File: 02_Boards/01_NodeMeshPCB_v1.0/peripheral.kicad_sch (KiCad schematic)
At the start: 3 parts, among them U1 BME280

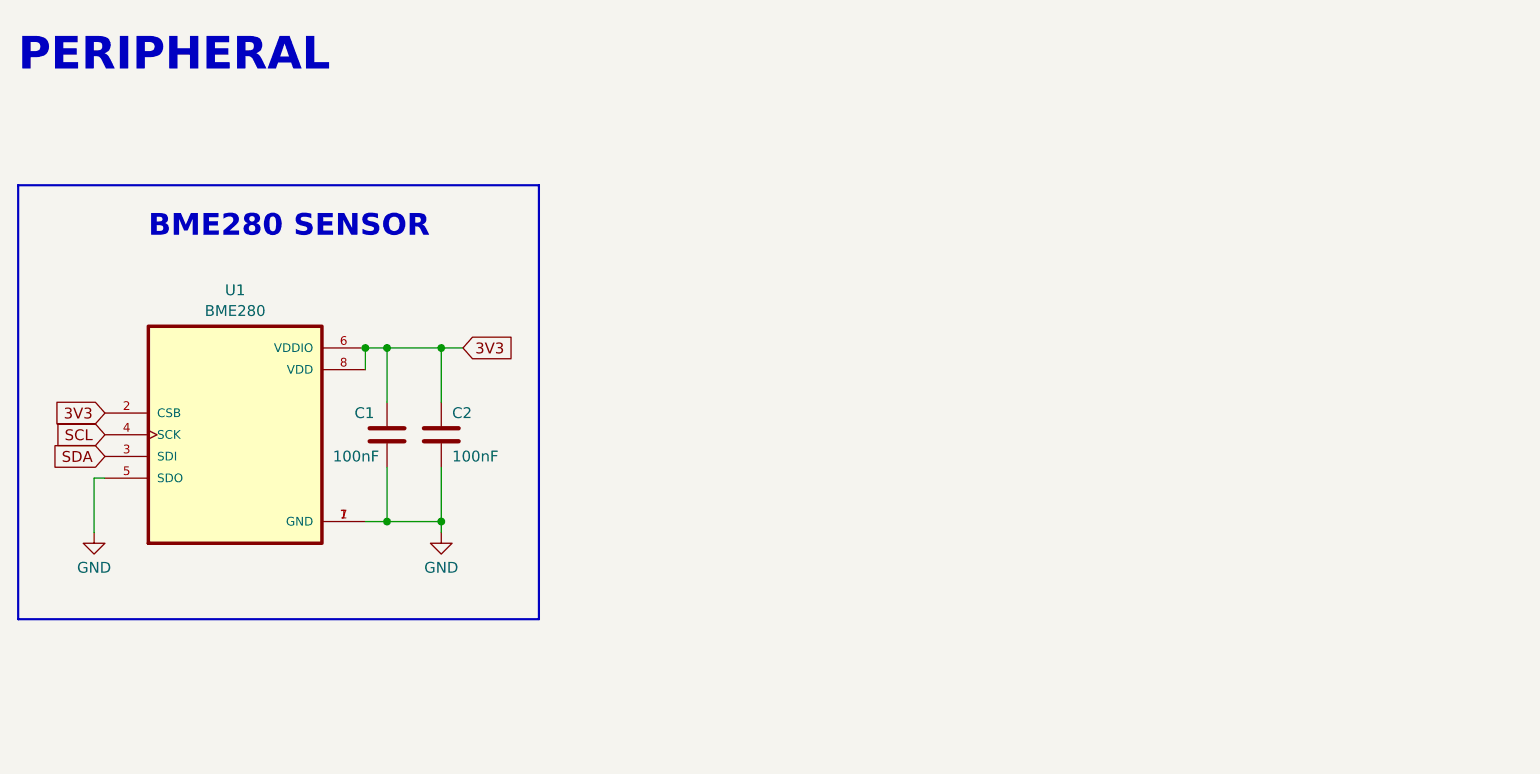
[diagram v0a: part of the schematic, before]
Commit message: INA3221 schematic
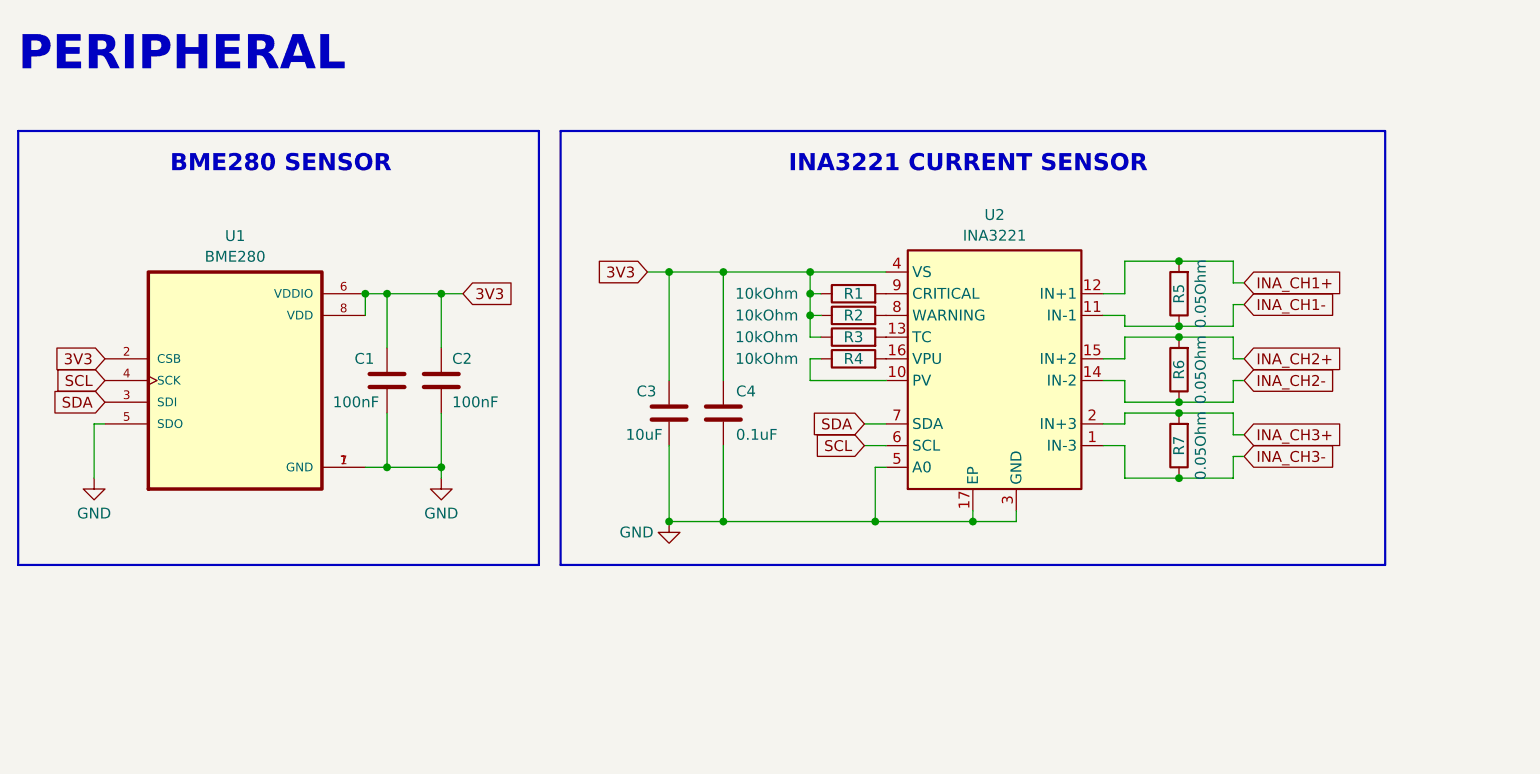
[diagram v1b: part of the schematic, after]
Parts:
- added C3: 10uF, symbol Device:C
- added C4: 0.1uF, symbol Device:C
- added R1, R2, R3, R4: 10kOhm, symbol Device:R
- added R5, R6, R7: 0.05Ohm, symbol Device:R
- added U2: INA3221, Package_DFN_QFN:Texas_RGV0016A_VQFN-16-1EP_4x4mm_P0.65mm_EP2.1x2.1mm, symbol INA3221:INA3221
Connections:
- net 3V3: now also C3.1, C4.1, R1.1, R2.1, R3.1, U2.4 (VS)
- net GND: now also C3.2, C4.2, U2.17 (EP), U2.3 (GND), U2.5 (A0)
- net SCL: now also U2.6 (SCL)
- net SDA: now also U2.7 (SDA)
- new net: R3.2, U2.13 (TC)
- new net: R4.1, U2.10 (PV)
- new net: R4.2, U2.16 (VPU)
- new net: R2.2, U2.8 (WARNING)
- new net: R1.2, U2.9 (CRITICAL)
- new net INA_CH1+: R5.2, U2.12 (IN+1)
- new net INA_CH1-: R5.1, U2.11 (IN-1)
- new net INA_CH2+: R6.2, U2.15 (IN+2)
- new net INA_CH2-: R6.1, U2.14 (IN-2)
- new net INA_CH3+: R7.2, U2.2 (IN+3)
- new net INA_CH3-: R7.1, U2.1 (IN-3)
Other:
- note added: "INA3221 CURRENT SENSOR"
- moved on the sheet: C1, C2, U1

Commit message: mppt solar charger schematic
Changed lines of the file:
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@@
+	(wire
+		(pts
+			(xy 77.47 71.12) (xy 74.93 71.12)
+		)
+		(stroke
+			(width 0)
+			(type default)
+		)
+	)
 	(wire
 		(pts
@@
 			(effects
 				(font
+					(size 1.27 1.27)
+				)
+				(justify left)
+				(hide yes)
+			)
+		)
+	)
+	(global_label "GND"
+		(shape input)
+		(at 77.47 71.12 0)
+		(fields_autoplaced yes)
+		(effects
+			(font
+				(size 1.27 1.27)
+			)
+			(justify left)
+		)
+		(property "Intersheetrefs" "${INTERSHEET_REFS}"
+			(at 84.3257 71.12 0)
+			(effects
+				(font

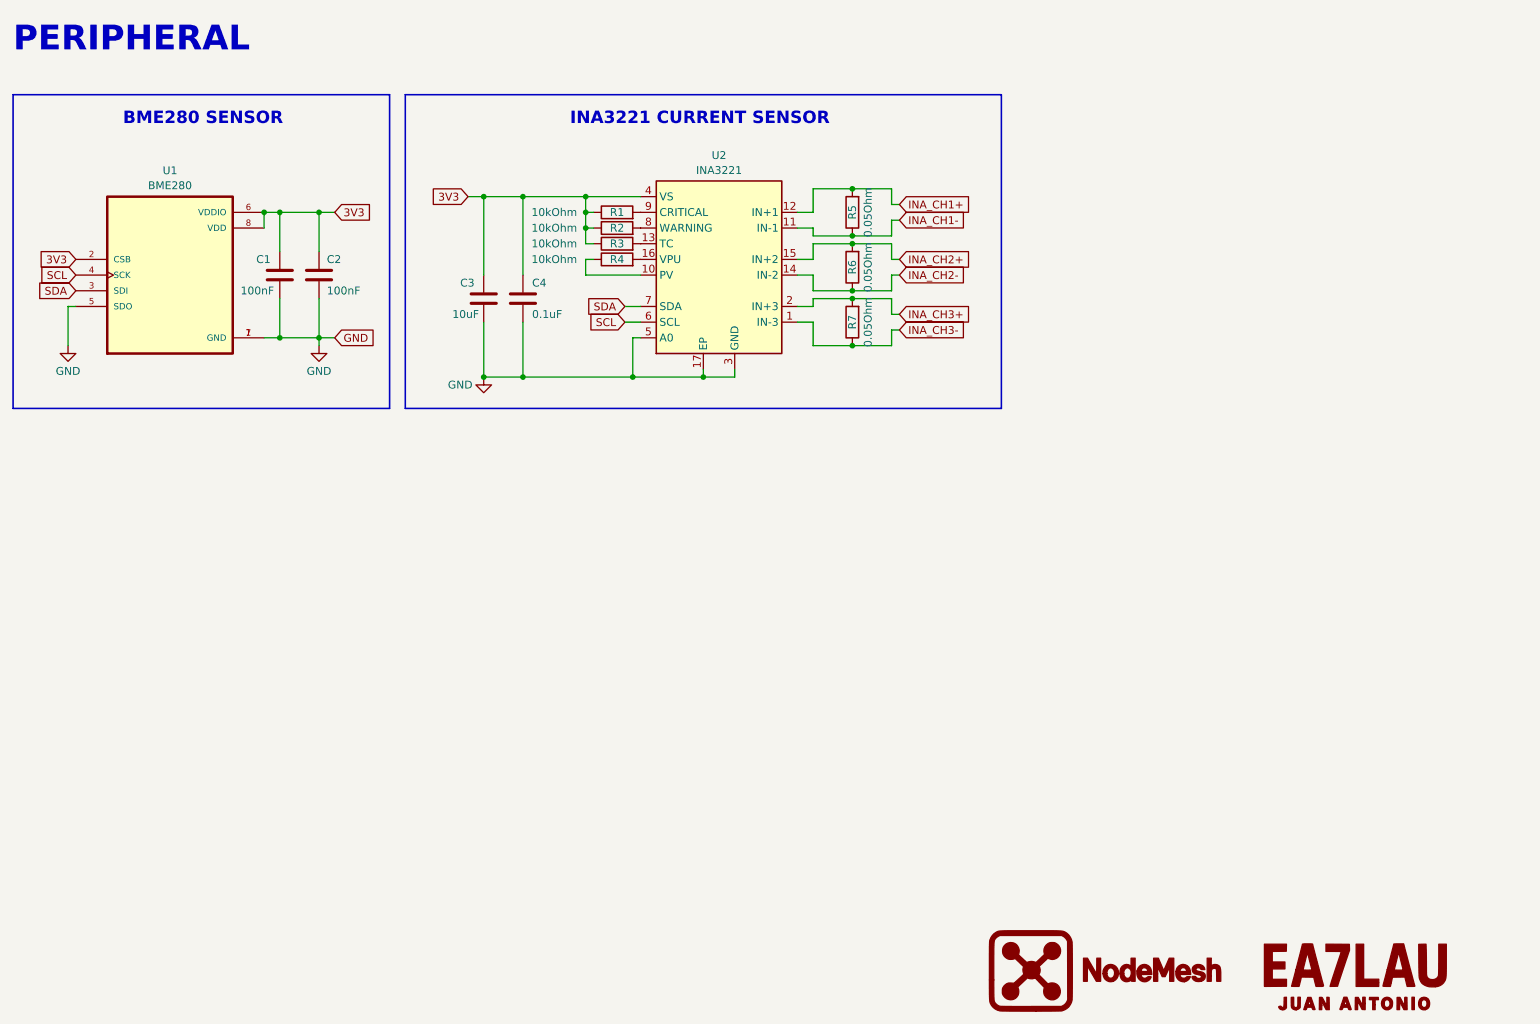
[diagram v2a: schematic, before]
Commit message: Control Mosfets Shematic
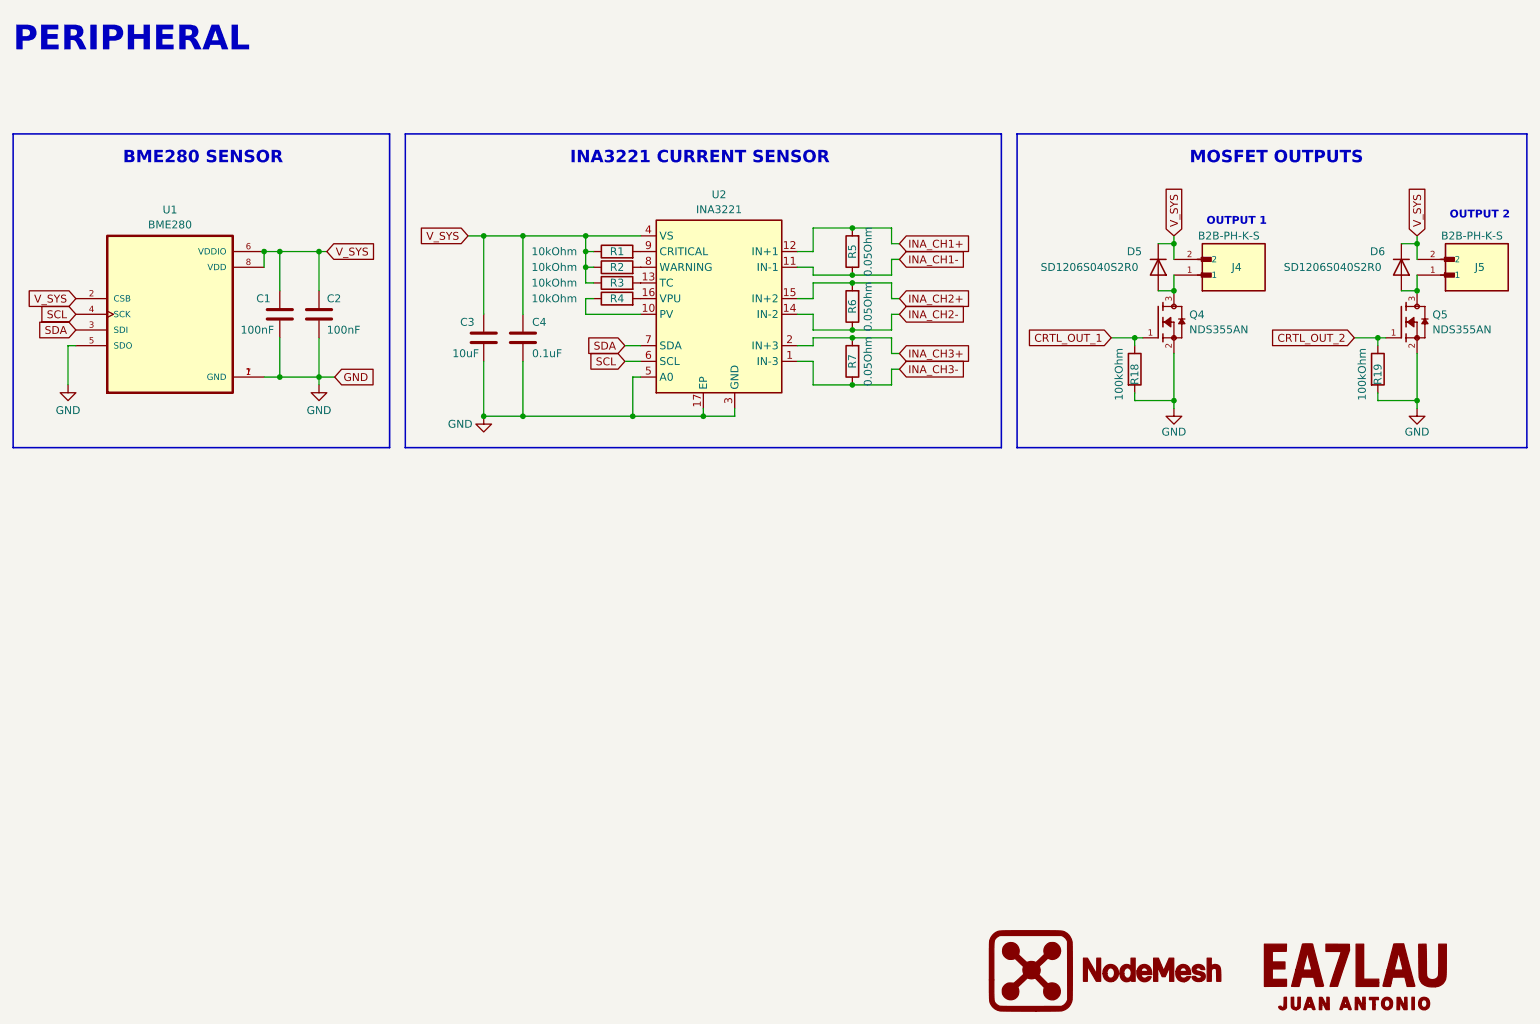
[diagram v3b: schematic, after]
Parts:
- added D5, D6: SD1206S040S2R0, Diode_SMD:D_1206_3216Metric, symbol Device:D
- added J4, J5: B2B-PH-K-S, B2B-PH-K-S:JST_B2B-PH-K-S, symbol B2B-PH-K-S:B2B-PH-K-S
- added Q4, Q5: NDS355AN, NDS355AN:SOT95P251X112-3N, symbol NDS355AN:NDS355AN
- added R18, R19: 100kOhm, symbol Device:R
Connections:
- net GND: now also Q4.2, Q5.2, R18.2, R19.2
- net 3V3 renamed V_SYS
- net V_SYS: now also D5.1 (K), D6.1 (K), J4.2, J5.2
- new net: D5.2 (A), J4.1, Q4.3
- new net: D6.2 (A), J5.1, Q5.3
- new net CRTL_OUT_1: Q4.1, R18.1
- new net CRTL_OUT_2: Q5.1, R19.1
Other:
- note added: "MOSFET OUTPUTS"
- note added: "OUTPUT 1"
- note added: "OUTPUT 2"
- moved on the sheet: C1, C2, C3, C4, R1, R2, R3, R4, R5, R6, R7, U1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

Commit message: ht-ra62 schematic
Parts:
- renumbered C1 to C13, C2 to C14, C3 to C15, C4 to C16, R1 to R10, R2 to R11, R3 to R12, R4 to R13, R5 to R14, R6 to R15, R7 to R16, R18 to R17, R19 to R18, U1 to U6, U2 to U7
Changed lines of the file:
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@@
 	)
 	(junction
-		(at 66.04 57.15)
+		(at 107.95 83.82)
 		(diameter 0)
 		(color 0 0 0 0)
 	)
 	(junction
-		(at 107.95 83.82)
+		(at 252.73 55.88)
 		(diameter 0)
 		(color 0 0 0 0)
 	)
 	(junction
-		(at 252.73 55.88)
+		(at 68.58 59.69)
 		(diameter 0)
 		(color 0 0 0 0)
@@
 	(wire
 		(pts
+			(xy 68.58 59.69) (xy 68.58 63.5)
+		)
+		(stroke
+			(width 0)
+			(type default)
+		)
+	)
+	(wire
+		(pts
 			(xy 207.01 81.28) (xy 213.36 81.28)
 		)
@@
 	(wire
 		(pts
+			(xy 66.04 59.69) (xy 68.58 59.69)
+		)
+		(stroke
+			(width 0)
+			(type default)
+		)
+	)
+	(wire
+		(pts
 			(xy 154.94 53.34) (xy 161.29 53.34)
 		)
@@
 	(wire
 		(pts
-			(xy 68.58 57.15) (xy 68.58 63.5)
+			(xy 68.58 57.15) (xy 68.58 59.69)
 		)
 		(stroke
@@
 	(wire
 		(pts
-			(xy 66.04 57.15) (xy 66.04 59.69)
-		)
-		(stroke
-			(width 0)
-			(type default)
-		)
-	)
-	(wire
-		(pts
 			(xy 207.01 72.39) (xy 207.01 71.12)
 		)
@@
 		(on_board yes)
 		(dnp no)
-		(property "Reference" "#PWR032"
+		(property "Reference" "#PWR05"
 			(at 213.36 88.9 0)
 			(effects
@@
 			(project "01_NodeMeshPCB_v1.0"
 				(path "/1ce5abde-bad5-41d0-ae59-b000d0618a73/9d46fcdc-bcd3-4b26-b047-a5216822dc91"
-					(reference "#PWR032")
+					(reference "#PWR05")
 					(unit 1)
 				)
@@
 		(on_board yes)
 		(dnp no)
-		(property "Reference" "R3"
+		(property "Reference" "R12"
 			(at 123.19 62.23 90)
 			(effects
@@
 			(project "01_NodeMeshPCB_v1.0"
 				(path "/1ce5abde-bad5-41d0-ae59-b000d0618a73/9d46fcdc-bcd3-4b26-b047-a5216822dc91"
-					(reference "R3")
+					(reference "R12")
 					(unit 1)
 				)
@@
 		(dnp no)
 		(fields_autoplaced yes)
-		(property "Reference" "U1"
+		(property "Reference" "U6"
 			(at 50.8 50.3893 0)
 			(effects
@@
 			(project ""
 				(path "/1ce5abde-bad5-41d0-ae59-b000d0618a73/9d46fcdc-bcd3-4b26-b047-a5216822dc91"
-					(reference "U1")
+					(reference "U6")
 					(unit 1)
 				)
@@
 		(dnp no)
 		(fields_autoplaced yes)
-		(property "Reference" "#PWR01"
+		(property "Reference" "#PWR03"
 			(at 74.93 85.09 0)
 			(effects
@@
 			(project ""
 				(path "/1ce5abde-bad5-41d0-ae59-b000d0618a73/9d46fcdc-bcd3-4b26-b047-a5216822dc91"
-					(reference "#PWR01")
+					(reference "#PWR03")
 					(unit 1)
 				)
@@
 		(dnp no)
 		(fields_autoplaced yes)
-		(property "Reference" "U2"
+		(property "Reference" "U7"
 			(at 139.7 47.9255 0)
 			(effects
@@
 			(project ""
 				(path "/1ce5abde-bad5-41d0-ae59-b000d0618a73/9d46fcdc-bcd3-4b26-b047-a5216822dc91"
-					(reference "U2")
+					(reference "U7")
 					(unit 1)
 				)
@@
 		(on_board yes)
 		(dnp no)
-		(property "Reference" "R7"
+		(property "Reference" "R16"
 			(at 161.29 74.93 90)
 			(effects
@@
 			(project "01_NodeMeshPCB_v1.0"
 				(path "/1ce5abde-bad5-41d0-ae59-b000d0618a73/9d46fcdc-bcd3-4b26-b047-a5216822dc91"
-					(reference "R7")
+					(reference "R16")
 					(unit 1)
 				)
@@
 		(on_board yes)
 		(dnp no)
-		(property "Reference" "R18"
+		(property "Reference" "R17"
 			(at 207.01 78.74 90)
 			(effects
@@
 			(project "01_NodeMeshPCB_v1.0"
 				(path "/1ce5abde-bad5-41d0-ae59-b000d0618a73/9d46fcdc-bcd3-4b26-b047-a5216822dc91"
-					(reference "R18")
+					(reference "R17")
 					(unit 1)
 				)
@@
 		(on_board yes)
 		(dnp no)
-		(property "Reference" "C1"
+		(property "Reference" "C13"
 			(at 64.77 64.77 0)
 			(effects
@@
 			(project ""
 				(path "/1ce5abde-bad5-41d0-ae59-b000d0618a73/9d46fcdc-bcd3-4b26-b047-a5216822dc91"
-					(reference "C1")
+					(reference "C13")
 					(unit 1)
 				)
@@
 		(on_board yes)
 		(dnp no)
-		(property "Reference" "C4"
+		(property "Reference" "C16"
 			(at 111.76 68.58 0)
 			(effects
@@
 			(project "01_NodeMeshPCB_v1.0"
 				(path "/1ce5abde-bad5-41d0-ae59-b000d0618a73/9d46fcdc-bcd3-4b26-b047-a5216822dc91"
-					(reference "C4")
+					(reference "C16")
 					(unit 1)
 				)
@@
 		(on_board yes)
 		(dnp no)
-		(property "Reference" "R4"
+		(property "Reference" "R13"
 			(at 123.19 64.77 90)
 			(effects
@@
 			(project "01_NodeMeshPCB_v1.0"
 				(path "/1ce5abde-bad5-41d0-ae59-b000d0618a73/9d46fcdc-bcd3-4b26-b047-a5216822dc91"
-					(reference "R4")
+					(reference "R13")
 					(unit 1)
 				)
@@
 		(on_board yes)
 		(dnp no)
-		(property "Reference" "R2"
+		(property "Reference" "R11"
 			(at 123.19 59.69 90)
 			(effects
@@
 			(project "01_NodeMeshPCB_v1.0"
 				(path "/1ce5abde-bad5-41d0-ae59-b000d0618a73/9d46fcdc-bcd3-4b26-b047-a5216822dc91"
-					(reference "R2")
+					(reference "R11")
 					(unit 1)
 				)
@@
 		(on_board yes)
 		(dnp no)
-		(property "Reference" "C2"
+		(property "Reference" "C14"
 			(at 76.2 64.77 0)
 			(effects
@@
 			(project "01_NodeMeshPCB_v1.0"
 				(path "/1ce5abde-bad5-41d0-ae59-b000d0618a73/9d46fcdc-bcd3-4b26-b047-a5216822dc91"
-					(reference "C2")
+					(reference "C14")
 					(unit 1)
 				)
@@
 		(on_board yes)
 		(dnp no)
-		(property "Reference" "#PWR033"
+		(property "Reference" "#PWR06"
 			(at 252.73 88.9 0)
 			(effects
@@
 			(project "01_NodeMeshPCB_v1.0"
 				(path "/1ce5abde-bad5-41d0-ae59-b000d0618a73/9d46fcdc-bcd3-4b26-b047-a5216822dc91"
-					(reference "#PWR033")
+					(reference "#PWR06")
 					(unit 1)
 				)
@@
 		(on_board yes)
 		(dnp no)
-		(property "Reference" "R5"
+		(property "Reference" "R14"
 			(at 161.29 57.15 90)
 			(effects
@@
 			(project "01_NodeMeshPCB_v1.0"
 				(path "/1ce5abde-bad5-41d0-ae59-b000d0618a73/9d46fcdc-bcd3-4b26-b047-a5216822dc91"
-					(reference "R5")
+					(reference "R14")
 					(unit 1)
 				)
@@
 		(on_board yes)
 		(dnp no)
-		(property "Reference" "R6"
+		(property "Reference" "R15"
 			(at 161.29 66.04 90)
 			(effects
@@
 			(project "01_NodeMeshPCB_v1.0"
 				(path "/1ce5abde-bad5-41d0-ae59-b000d0618a73/9d46fcdc-bcd3-4b26-b047-a5216822dc91"
-					(reference "R6")
+					(reference "R15")
 					(unit 1)
 				)
@@
 		(on_board yes)
 		(dnp no)
-		(property "Reference" "C3"
+		(property "Reference" "C15"
 			(at 97.79 68.58 0)
 			(effects
@@
 			(project ""
 				(path "/1ce5abde-bad5-41d0-ae59-b000d0618a73/9d46fcdc-bcd3-4b26-b047-a5216822dc91"
-					(reference "C3")
+					(reference "C15")
 					(unit 1)
 				)
@@
 		(on_board yes)
 		(dnp no)
-		(property "Reference" "#PWR03"
+		(property "Reference" "#PWR04"
 			(at 101.6 90.17 0)
 			(effects
@@
 			(project "01_NodeMeshPCB_v1.0"
 				(path "/1ce5abde-bad5-41d0-ae59-b000d0618a73/9d46fcdc-bcd3-4b26-b047-a5216822dc91"
-					(reference "#PWR03")
+					(reference "#PWR04")
 					(unit 1)
 				)
@@
 		(on_board yes)
 		(dnp no)
-		(property "Reference" "R19"
+		(property "Reference" "R18"
 			(at 246.38 78.74 90)
 			(effects
@@
 			(project "01_NodeMeshPCB_v1.0"
 				(path "/1ce5abde-bad5-41d0-ae59-b000d0618a73/9d46fcdc-bcd3-4b26-b047-a5216822dc91"
-					(reference "R19")
+					(reference "R18")
 					(unit 1)
 				)
@@
 		(on_board yes)
 		(dnp no)
-		(property "Reference" "R1"
+		(property "Reference" "R10"
 			(at 123.19 57.15 90)
 			(effects
@@
 			(project ""
 				(path "/1ce5abde-bad5-41d0-ae59-b000d0618a73/9d46fcdc-bcd3-4b26-b047-a5216822dc91"
-					(reference "R1")
+					(reference "R10")
 					(unit 1)
 				)

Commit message: PCB placement
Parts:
- added J10: 61300411121, 01_Footprints:61300411121, symbol 61300411121:61300411121
- C39: renamed from C13; footprint (none) -> Capacitor_SMD:C_0603_1608Metric
- C40: renamed from C14; footprint (none) -> Capacitor_SMD:C_0603_1608Metric
- C41: renamed from C15; footprint (none) -> Capacitor_SMD:C_0603_1608Metric
- C42: renamed from C16; footprint (none) -> Capacitor_SMD:C_0603_1608Metric
- J8: renamed from J4; value B2B-PH-K-S -> 1751248; footprint B2B-PH-K-S:JST_B2B-PH-K-S -> TerminalBlock_Phoenix:TerminalBlock_Phoenix_MKDS-1,5-2-5.08_1x02_P5.08mm_Horizontal
- J9: renamed from J5; value B2B-PH-K-S -> 1751248; footprint B2B-PH-K-S:JST_B2B-PH-K-S -> TerminalBlock_Phoenix:TerminalBlock_Phoenix_MKDS-1,5-2-5.08_1x02_P5.08mm_Horizontal
- Q5: renamed from Q4; footprint NDS355AN:SOT95P251X112-3N -> 01_Footprints:NDS355AN
- Q6: renamed from Q5; footprint NDS355AN:SOT95P251X112-3N -> 01_Footprints:NDS355AN
- R29: renamed from R10; footprint (none) -> Resistor_SMD:R_0603_1608Metric
- R30: renamed from R14; footprint (none) -> Resistor_SMD:R_1206_3216Metric
- R31: renamed from R11; footprint (none) -> Resistor_SMD:R_0603_1608Metric
- R32: renamed from R12; footprint (none) -> Resistor_SMD:R_0603_1608Metric
- R33: renamed from R13; footprint (none) -> Resistor_SMD:R_0603_1608Metric
- R34: renamed from R15; footprint (none) -> Resistor_SMD:R_1206_3216Metric
- R35: renamed from R16; footprint (none) -> Resistor_SMD:R_1206_3216Metric
- R36: renamed from R17; footprint (none) -> Resistor_SMD:R_0603_1608Metric
- R37: renamed from R18; footprint (none) -> Resistor_SMD:R_0603_1608Metric
- U10: renamed from U7; footprint Package_DFN_QFN:Texas_RGV0016A_VQFN-16-1EP_4x4mm_P0.65mm_EP2.1x2.1mm -> 01_Footprints:INA3221
- U9: renamed from U6; footprint BME280:PSON65P250X250X100-8N -> 01_Footprints:BME280
- renumbered D5 to D6, D6 to D7
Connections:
- net GND: now also J10.1
- net SCL: now also J10.4
- net SDA: now also J10.3
- net V_SYS: now also J10.2
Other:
- note added: "OLED SCREEN CONNECTOR"
